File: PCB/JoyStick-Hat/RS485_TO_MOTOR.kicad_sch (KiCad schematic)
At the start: 8 parts, among them U4 MAX3535ECWI+T

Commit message: Board Tweaks and progress
Made progress with baord. Adjusted the position of RPi header to be correct and absolute. Changed location of regulator modules and power input capacitors. Added 3D models missing from the larger components. Changed connectors and positions for just about everything. Added connnector for LED driver duagher board .
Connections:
- net at U4.2 (ST1): now also L3.3; no longer L3.1
- net at U4.3 (ST2): now also L3.1; no longer L3.3
- net at D13.1: now also L3.4; no longer L3.6
- net at D13.2: now also L3.6; no longer L3.4
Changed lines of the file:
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@@
   (symbol (lib_id "AVR-KiCAD-Lib-Capacitors:CL10B104JB8NNNC") (at 201.93 68.58 90) (unit 1)
     (in_bom yes) (on_board yes) (dnp no) (fields_autoplaced)
-    (property "Reference" "C?" (at 198.12 66.675 90)
+    (property "Reference" "C27" (at 198.12 66.675 90)
       (effects (font (size 1.27 1.27)) (justify left))
     )
@@
   (symbol (lib_id "AVR-KiCAD-Lib-Capacitors:CL10B104JB8NNNC") (at 107.95 69.85 90) (unit 1)
     (in_bom yes) (on_board yes) (dnp no) (fields_autoplaced)
-    (property "Reference" "C?" (at 104.14 67.945 90)
+    (property "Reference" "C25" (at 104.14 67.945 90)
       (effects (font (size 1.27 1.27)) (justify left))
     )
@@
     )
   )
-  (symbol (lib_id "AVR-KiCAD-Lib-Transformers:Q4470-CL") (at 156.21 67.31 0) (unit 1)
-    (in_bom yes) (on_board yes) (dnp no) (fields_autoplaced)
-    (property "Reference" "L3" (at 156.21 57.15 0)
-      (effects (font (size 1.27 1.27)))
-    )
-    (property "Value" "Q4470-CL" (at 156.21 74.93 0)
-      (effects (font (size 1.27 1.27)) hide)
-    )
-    (property "Footprint" "AVR-KiCAD-Lib-Transformers:SO6_Q4470-CL_C-SIZE_COC" (at 160.0621 67.2679 90)
-      (effects (font (size 1.27 1.27)) hide)
-    )
-    (property "Datasheet" "https://www.coilcraft.com/getmedia/97b6ad34-63ed-485c-a3ac-2a258e22c8ff/mintrans.pdf" (at 160.0621 67.2679 90)
-      (effects (font (size 1.27 1.27)) hide)
-    )
-    (property "Cost QTY: 1" "$2.12 " (at 158.75 60.96 0)
-      (effects (font (size 1.27 1.27)) hide)
-    )
-    (property "Cost QTY: 1000" "$1.38 " (at 161.29 58.42 0)
-      (effects (font (size 1.27 1.27)) hide)
-    )
-    (property "Cost QTY: 2500" "*" (at 163.83 55.88 0)
-      (effects (font (size 1.27 1.27)) hide)
-    )
-    (property "Cost QTY: 5000" "$1.09 " (at 166.37 53.34 0)
-      (effects (font (size 1.27 1.27)) hide)
-    )
-    (property "Cost QTY: 10000" "*" (at 168.91 50.8 0)
-      (effects (font (size 1.27 1.27)) hide)
-    )
-    (property "MFR" "Coilcraft" (at 171.45 48.26 0)
-      (effects (font (size 1.27 1.27)) hide)
-    )
-    (property "MFR#" "Q4470-CL" (at 173.99 45.72 0)
-      (effects (font (size 1.27 1.27)) hide)
-    )
-    (property "Vendor" "Coilcraft" (at 176.53 43.18 0)
-      (effects (font (size 1.27 1.27)) hide)
-    )
-    (property "Vendor #" "Q4470-CL" (at 179.07 40.64 0)
-      (effects (font (size 1.27 1.27)) hide)
-    )
-    (property "Designer" "Adam Vadala-Roth" (at 181.61 38.1 0)
-      (effects (font (size 1.27 1.27)) hide)
-    )
-    (property "Height" "5.46mm" (at 184.15 35.56 0)
-      (effects (font (size 1.27 1.27)) hide)
-    )
-    (property "Date Created" "11/11/2023" (at 212.09 7.62 0)
-      (effects (font (size 1.27 1.27)) hide)
-    )
-    (property "Date Modified" "11/11/2023" (at 186.69 33.02 0)
-      (effects (font (size 1.27 1.27)) hide)
-    )
-    (property "Lead-Free ?" "Yes" (at 189.23 30.48 0)
-      (effects (font (size 1.27 1.27)) hide)
-    )
-    (property "RoHS Levels" "1" (at 191.77 27.94 0)
-      (effects (font (size 1.27 1.27)) hide)
-    )
-    (property "Mounting" "SMT" (at 194.31 25.4 0)
-      (effects (font (size 1.27 1.27)) hide)
-    )
-    (property "Pin Count #" "6" (at 196.85 22.86 0)
-      (effects (font (size 1.27 1.27)) hide)
-    )
-    (property "Status" "Active" (at 199.39 20.32 0)
-      (effects (font (size 1.27 1.27)) hide)
-    )
-    (property "Tolerance" "*" (at 201.93 17.78 0)
-      (effects (font (size 1.27 1.27)) hide)
-    )
-    (property "Type" "Transformer" (at 204.47 15.24 0)
-      (effects (font (size 1.27 1.27)) hide)
-    )
-    (property "Voltage" "5V" (at 207.01 12.7 0)
-      (effects (font (size 1.27 1.27)) hide)
-    )
-    (property "Package" "Proprietary" (at 209.55 8.89 0)
-      (effects (font (size 1.27 1.27)) hide)
-    )
-    (property "_Value_" "Q4470-CL" (at 156.21 59.69 0)
-      (effects (font (size 1.27 1.27)))
-    )
-    (property "Description" "miniature transformers were developed for use with" (at 154.94 58.42 90)
-      (effects (font (size 1.27 1.27)) hide)
-    )
-    (property "Management_ID" "Maxim RS-232/RS-485 interface ICs" (at 217.17 1.27 0)
-      (effects (font (size 1.27 1.27)) hide)
-    )
+  (symbol (lib_id "AVR-KiCAD-Lib-Transformers:Q4470-CL") (at 156.21 67.31 0) (mirror x) (unit 1)
+    (in_bom yes) (on_board yes) (dnp no)
+    (property "Reference" "L3" (at 156.21 77.47 0)
+      (effects (font (size 1.27 1.27)))
+    )
+    (property "Value" "Q4470-CL" (at 156.21 59.69 0)
+      (effects (font (size 1.27 1.27)) hide)
+    )
+    (property "Footprint" "AVR-KiCAD-Lib-Transformers:SO6_Q4470-CL_C-SIZE_COC" (at 160.0621 67.3521 90)
+      (effects (font (size 1.27 1.27)) hide)
+    )
+    (property "Datasheet" "https://www.coilcraft.com/getmedia/97b6ad34-63ed-485c-a3ac-2a258e22c8ff/mintrans.pdf" (at 160.0621 67.3521 90)
+      (effects (font (size 1.27 1.27)) hide)
+    )
+    (property "Cost QTY: 1" "$2.12 " (at 158.75 73.66 0)
+      (effects (font (size 1.27 1.27)) hide)
+    )
+    (property "Cost QTY: 1000" "$1.38 " (at 161.29 76.2 0)
+      (effects (font (size 1.27 1.27)) hide)
+    )
+    (property "Cost QTY: 2500" "*" (at 163.83 78.74 0)
+      (effects (font (size 1.27 1.27)) hide)
+    )
+    (property "Cost QTY: 5000" "$1.09 " (at 166.37 81.28 0)
+      (effects (font (size 1.27 1.27)) hide)
+    )
+    (property "Cost QTY: 10000" "*" (at 168.91 83.82 0)
+      (effects (font (size 1.27 1.27)) hide)
+    )
+    (property "MFR" "Coilcraft" (at 171.45 86.36 0)
+      (effects (font (size 1.27 1.27)) hide)
+    )
+    (property "MFR#" "Q4470-CL" (at 173.99 88.9 0)
+      (effects (font (size 1.27 1.27)) hide)
+    )
+    (property "Vendor" "Coilcraft" (at 176.53 91.44 0)
+      (effects (font (size 1.27 1.27)) hide)
+    )
+    (property "Vendor #" "Q4470-CL" (at 179.07 93.98 0)
+      (effects (font (size 1.27 1.27)) hide)
+    )
+    (property "Designer" "Adam Vadala-Roth" (at 181.61 96.52 0)
+      (effects (font (size 1.27 1.27)) hide)
+    )
+    (property "Height" "5.46mm" (at 184.15 99.06 0)
+      (effects (font (size 1.27 1.27)) hide)
+    )
+    (property "Date Created" "11/11/2023" (at 212.09 127 0)
+      (effects (font (size 1.27 1.27)) hide)
+    )
+    (property "Date Modified" "11/11/2023" (at 186.69 101.6 0)
+      (effects (font (size 1.27 1.27)) hide)
+    )
+    (property "Lead-Free ?" "Yes" (at 189.23 104.14 0)
+      (effects (font (size 1.27 1.27)) hide)
+    )
+    (property "RoHS Levels" "1" (at 191.77 106.68 0)
+      (effects (font (size 1.27 1.27)) hide)
+    )
+    (property "Mounting" "SMT" (at 194.31 109.22 0)
+      (effects (font (size 1.27 1.27)) hide)
+    )
+    (property "Pin Count #" "6" (at 196.85 111.76 0)
+      (effects (font (size 1.27 1.27)) hide)
+    )
+    (property "Status" "Active" (at 199.39 114.3 0)
+      (effects (font (size 1.27 1.27)) hide)
+    )
+    (property "Tolerance" "*" (at 201.93 116.84 0)
+      (effects (font (size 1.27 1.27)) hide)
+    )
+    (property "Type" "Transformer" (at 204.47 119.38 0)
+      (effects (font (size 1.27 1.27)) hide)
+    )
+    (property "Voltage" "5V" (at 207.01 121.92 0)
+      (effects (font (size 1.27 1.27)) hide)
+    )
+    (property "Package" "Proprietary" (at 209.55 125.73 0)
+      (effects (font (size 1.27 1.27)) hide)
+    )
+    (property "_Value_" "Q4470-CL" (at 156.21 74.93 0)
+      (effects (font (size 1.27 1.27)))
+    )
+    (property "Description" "miniature transformers were developed for use with" (at 154.94 76.2 90)
+      (effects (font (size 1.27 1.27)) hide)
+    )
+    (property "Management_ID" "Maxim RS-232/RS-485 interface ICs" (at 217.17 133.35 0)
+      (effects (font (size 1.27 1.27)) hide)
+    )

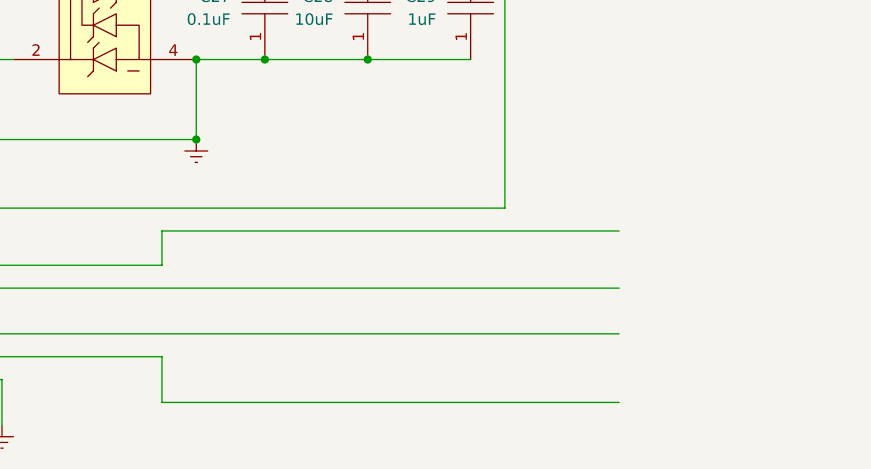
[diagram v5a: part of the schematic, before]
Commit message: Board Routing
Connectors swapped around and board route started
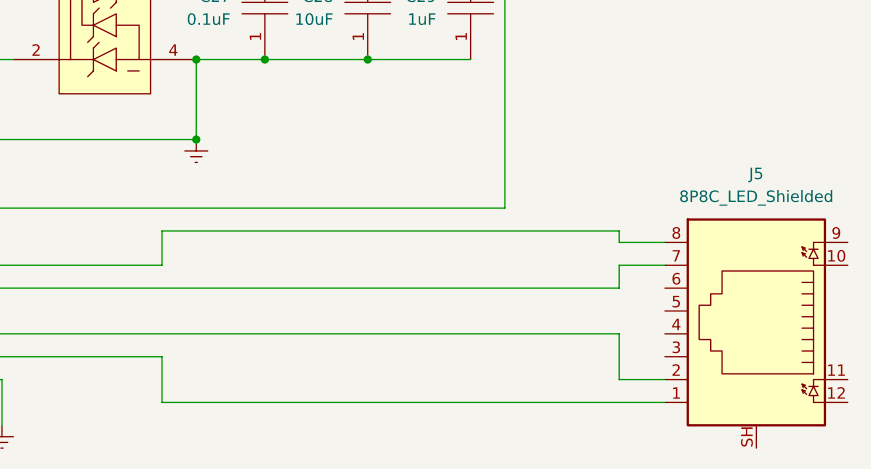
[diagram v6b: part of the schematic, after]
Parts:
- added J5: 8P8C_LED_Shielded, AVR-KiCAD-Lib-Connectors:RJ45_Wuerth_7499111446_Horizontal, symbol Connector:8P8C_LED_Shielded
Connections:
- net at U4.12 (Z): now also J5.1
- net at U4.13 (Y): now also J5.2
- net at U4.15 (B): now also J5.7
- net at U4.16 (A): now also J5.8
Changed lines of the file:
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@@
+    (stroke (width 0) (type default))
+  )
+  (wire (pts (xy 241.3 109.22) (xy 246.38 109.22))
     (stroke (width 0) (type default))
   )
@@
     (stroke (width 0) (type default))
   )
+  (wire (pts (xy 241.3 96.52) (xy 246.38 96.52))
+    (stroke (width 0) (type default))
+  )
   (wire (pts (xy 143.51 62.23) (xy 143.51 85.09))
     (stroke (width 0) (type default))
@@
     (stroke (width 0) (type default))
   )
+  (wire (pts (xy 241.3 93.98) (xy 246.38 93.98))
+    (stroke (width 0) (type default))
+  )
   (wire (pts (xy 127 96.52) (xy 127 63.5))
     (stroke (width 0) (type default))
@@
     (stroke (width 0) (type default))
   )
-  (wire (pts (xy 190.5 111.76) (xy 241.3 111.76))
+  (wire (pts (xy 190.5 111.76) (xy 246.38 111.76))
     (stroke (width 0) (type default))
   )
@@
     (stroke (width 0) (type default))
   )
+  (wire (pts (xy 241.3 92.71) (xy 241.3 93.98))
+    (stroke (width 0) (type default))
+  )
   (wire (pts (xy 228.6 90.17) (xy 228.6 62.23))
     (stroke (width 0) (type default))
@@
     (stroke (width 0) (type default))
   )
+  (wire (pts (xy 241.3 104.14) (xy 241.3 109.22))
+    (stroke (width 0) (type default))
+  )
   (wire (pts (xy 167.64 96.52) (xy 190.5 96.52))
+    (stroke (width 0) (type default))
+  )
+  (wire (pts (xy 241.3 99.06) (xy 241.3 96.52))
     (stroke (width 0) (type default))
   )
@@
         )
       )
+    )
+  )
+  (symbol (lib_id "Connector:8P8C_LED_Shielded") (at 256.54 104.14 0) (mirror y) (unit 1)
+    (in_bom yes) (on_board yes) (dnp no) (fields_autoplaced)
+    (property "Reference" "J5" (at 256.54 86.36 0)
+      (effects (font (size 1.27 1.27)))
+    )
+    (property "Value" "8P8C_LED_Shielded" (at 256.54 88.9 0)
+      (effects (font (size 1.27 1.27)))
+    )
+    (property "Footprint" "AVR-KiCAD-Lib-Connectors:RJ45_Wuerth_7499111446_Horizontal" (at 256.54 103.505 90)
+      (effects (font (size 1.27 1.27)) hide)
+    )
+    (property "Datasheet" "~" (at 256.54 103.505 90)
+      (effects (font (size 1.27 1.27)) hide)
+    )
+    (pin "2")
+    (pin "12")
+    (pin "5")
+    (pin "3")
+    (pin "4")
+    (pin "10")
+    (pin "11")
+    (pin "1")
+    (pin "6")
+    (pin "9")
+    (pin "SH")
+    (pin "7")
+    (pin "8")
+    (instances
+      (project "JoyStick-Hat"
+        (path "/cf0c81b5-5bdf-47c3-83c0-f6980f515e65/82e1f9af-1e5c-4e7f-8d36-34a266d2a8ff"
+          (reference "J5") (unit 1)
+        )
+      )

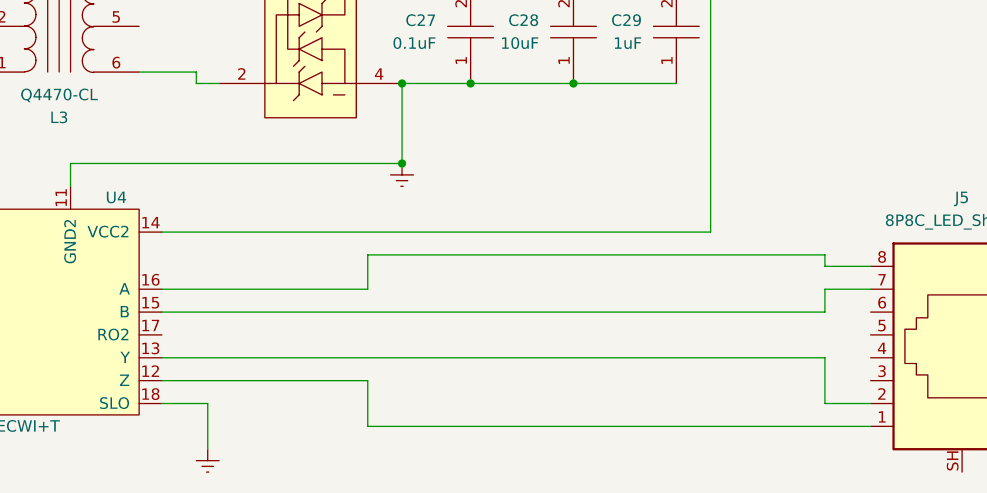
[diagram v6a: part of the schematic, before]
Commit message: James Fixes and 3D models
Added all the changes that James suggested to the design and then added 3D models to the board for mechanical design purposes. Generated 3D renders of the board and added them to new directory called img.
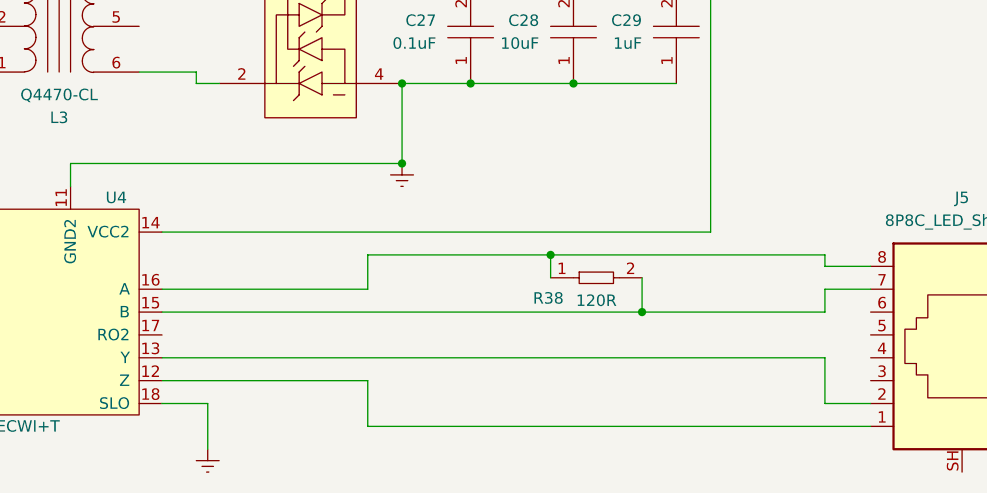
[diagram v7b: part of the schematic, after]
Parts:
- added R38: AC0402FR-07120RL, AVR-KiCAD-Lib-Resistors:R0402, symbol AVR-KiCAD-Lib-Resistors:AC0402FR-07120RL
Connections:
- net at J5.7, U4.15 (B): now also R38.2
- net at J5.8, U4.16 (A): now also R38.1

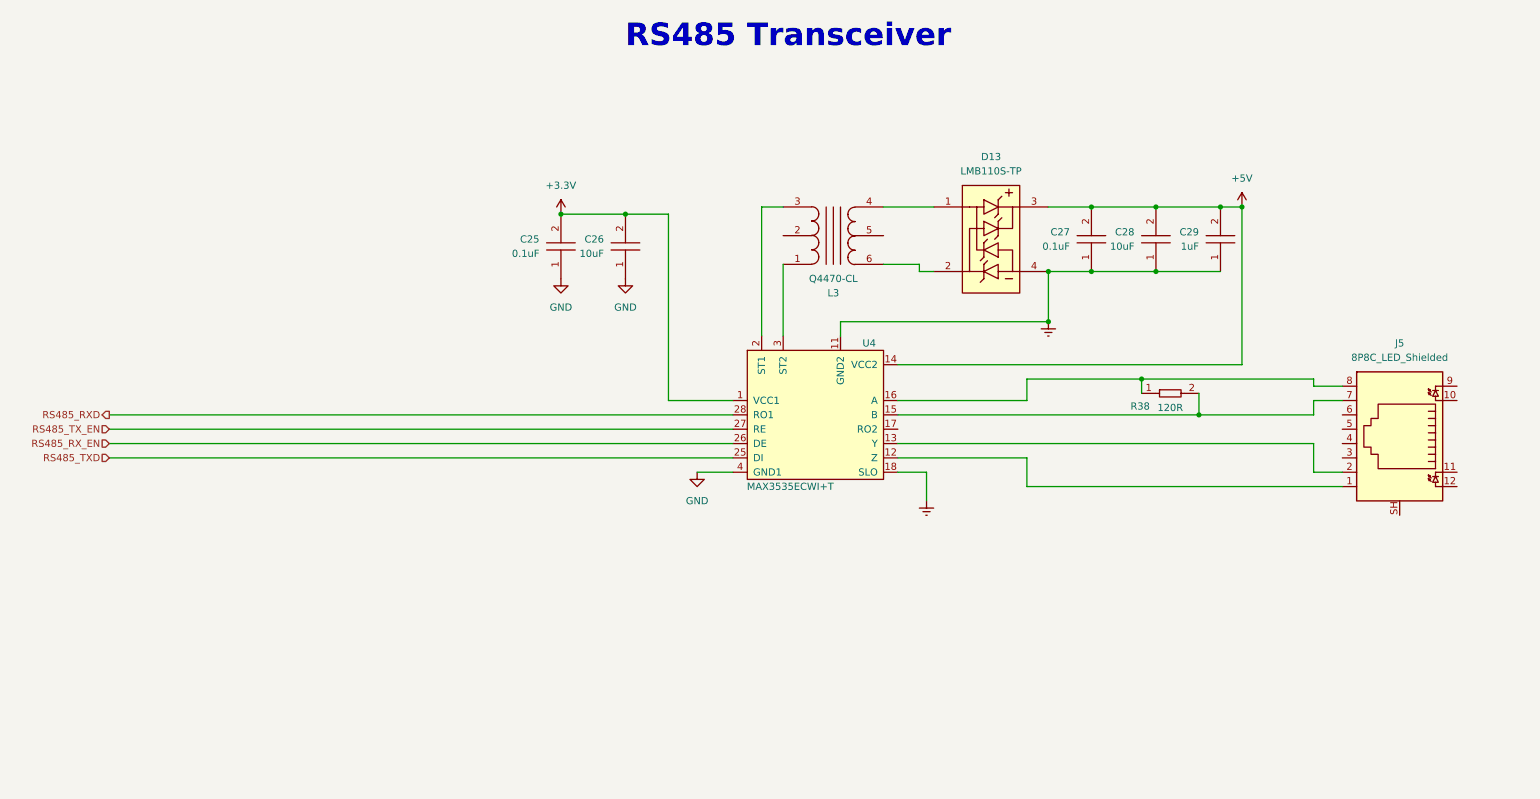
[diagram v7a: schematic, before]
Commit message: RJ45
Replaced RJ45 connector, original one had magnetics, those are not needed for RS485 and would have caused problems. Hooked up coms LEDs on RJ45 connector to MCU for debugging and displaying coms activity.
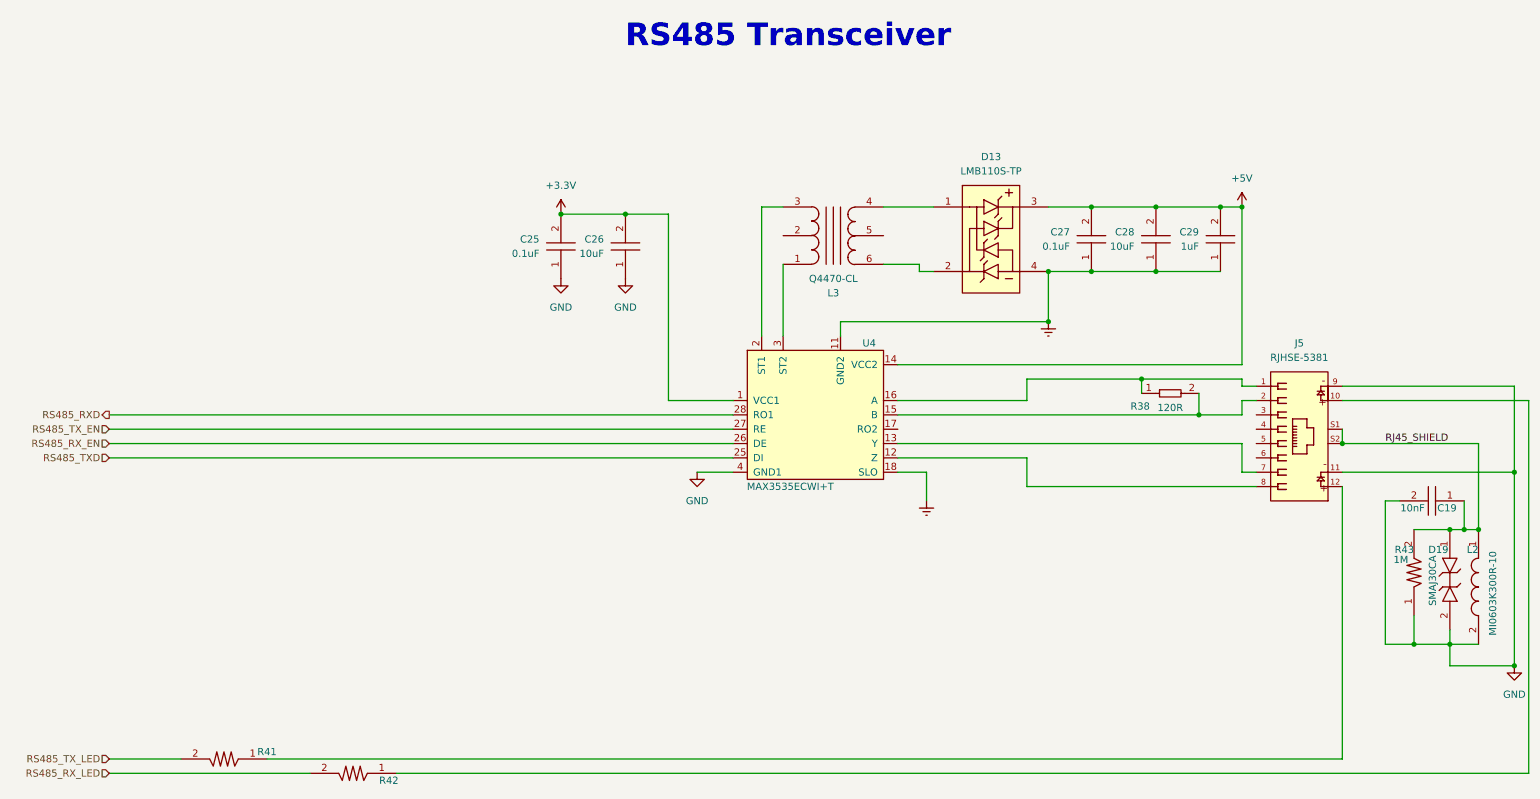
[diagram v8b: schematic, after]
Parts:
- removed J5: 8P8C_LED_Shielded, AVR-KiCAD-Lib-Connectors:RJ45_Wuerth_7499111446_Horizontal, symbol Connector:8P8C_LED_Shielded
- added C19: C0805C103KCRACAUTO, AVR-KiCAD-Lib-Capacitors:C0805, symbol AVR-KiCAD-Lib-Capacitors:C0805C103KCRACAUTO
- added D19: SMAJ30CA, AVR-KiCAD-Lib-Diodes:SMAJ30CA, symbol AVR-KiCAD-Lib-Diodes:SMAJ30CA
- added J5: RJHSE-5381, AVR-KiCAD-Lib-Connectors:AMPHENOL_RJHSE-5381, symbol AVR-KiCAD-Lib-Connectors:RJHSE-5381
- added L2: MI0603K300R-10, AVR-KiCAD-Lib-Inductors:MI0603K300R-10, symbol AVR-KiCAD-Lib-Inductors:MI0603K300R-10
- added R41, R42: RC0603FR-07470RL, AVR-KiCAD-Lib-Resistors:R0603, symbol AVR-KiCAD-Lib-Resistors:RC0603FR-07470RL
- added R43: RC1206FR-071ML, AVR-KiCAD-Lib-Resistors:R1206, symbol AVR-KiCAD-Lib-Resistors:RC1206FR-071ML
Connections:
- net GND: now also C19.2, D19.2, J5.11, J5.9, L2.2, R43.1
- net at U4.12 (Z): now also J5.8
- net at U4.13 (Y): now also J5.7
- net at R38.2, U4.15 (B): now also J5.2
- net at R38.1, U4.16 (A): now also J5.1
- new net: J5.10, R42.1
- new net: J5.12, R41.1
- new net RJ45_SHIELD: C19.1, D19.1, J5.S1, J5.S2, L2.1, R43.2
- new net RS485_RX_LED: R42.2
- new net RS485_TX_LED: R41.2
